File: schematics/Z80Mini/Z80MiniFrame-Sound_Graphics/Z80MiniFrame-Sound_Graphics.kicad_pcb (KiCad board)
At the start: 2 copper layers, 194.3 x 105.4 mm, 48 parts, among them J1 Conn_02x20_Odd_Even, J2 COMP_VIDEOUT, J3 Conn_01x03_Male, J4 IO_PORT, J5 COMP_VIDEOIN, Q1 2N3904, U1 TMS9918A, U12 74LS32, U2 74LS574, U3 74LS574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

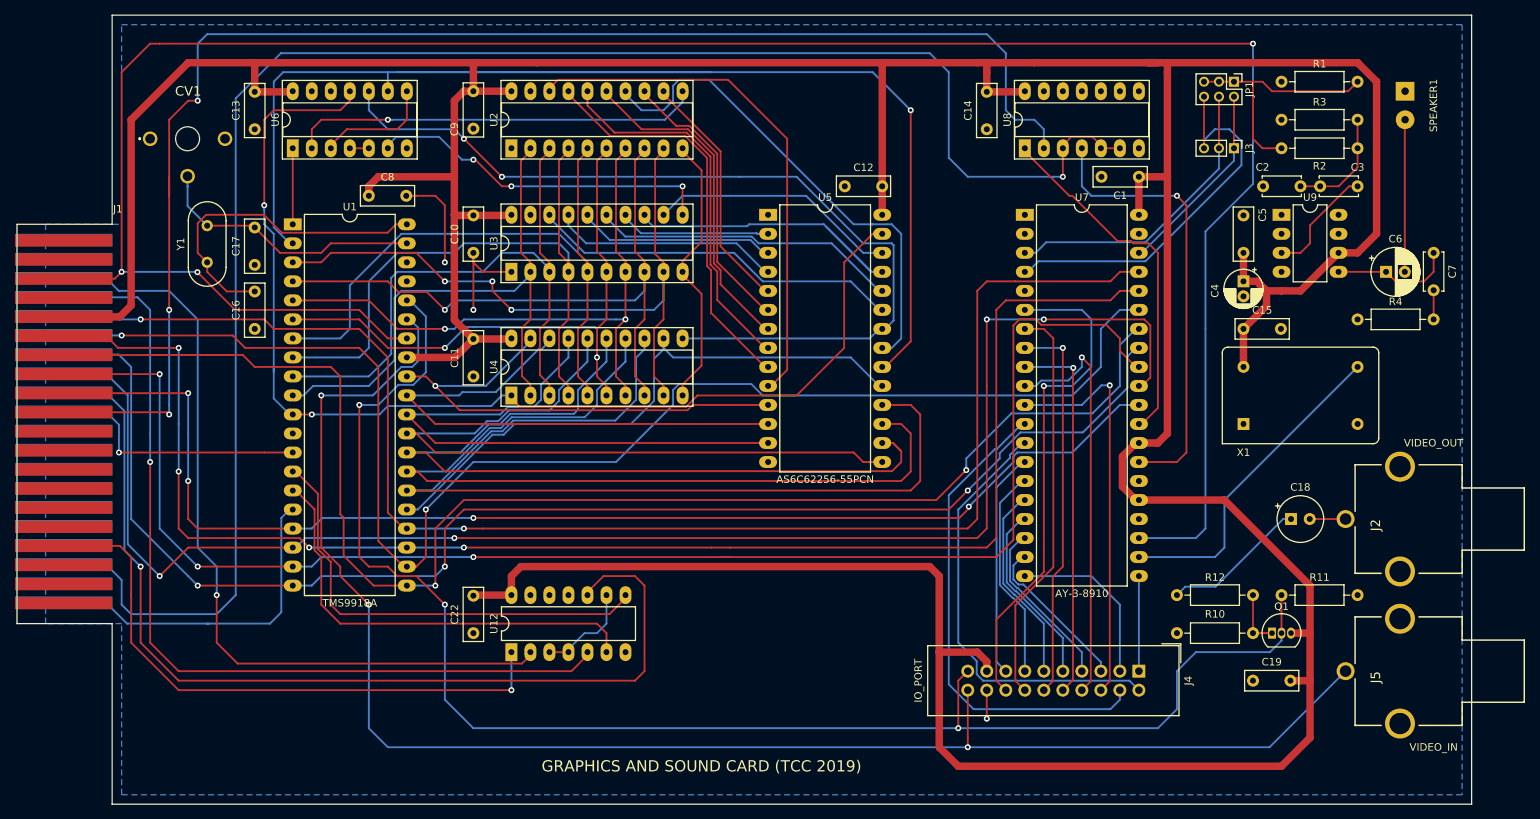
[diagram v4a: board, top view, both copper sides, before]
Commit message: Added new code for core written in C with Z88DK
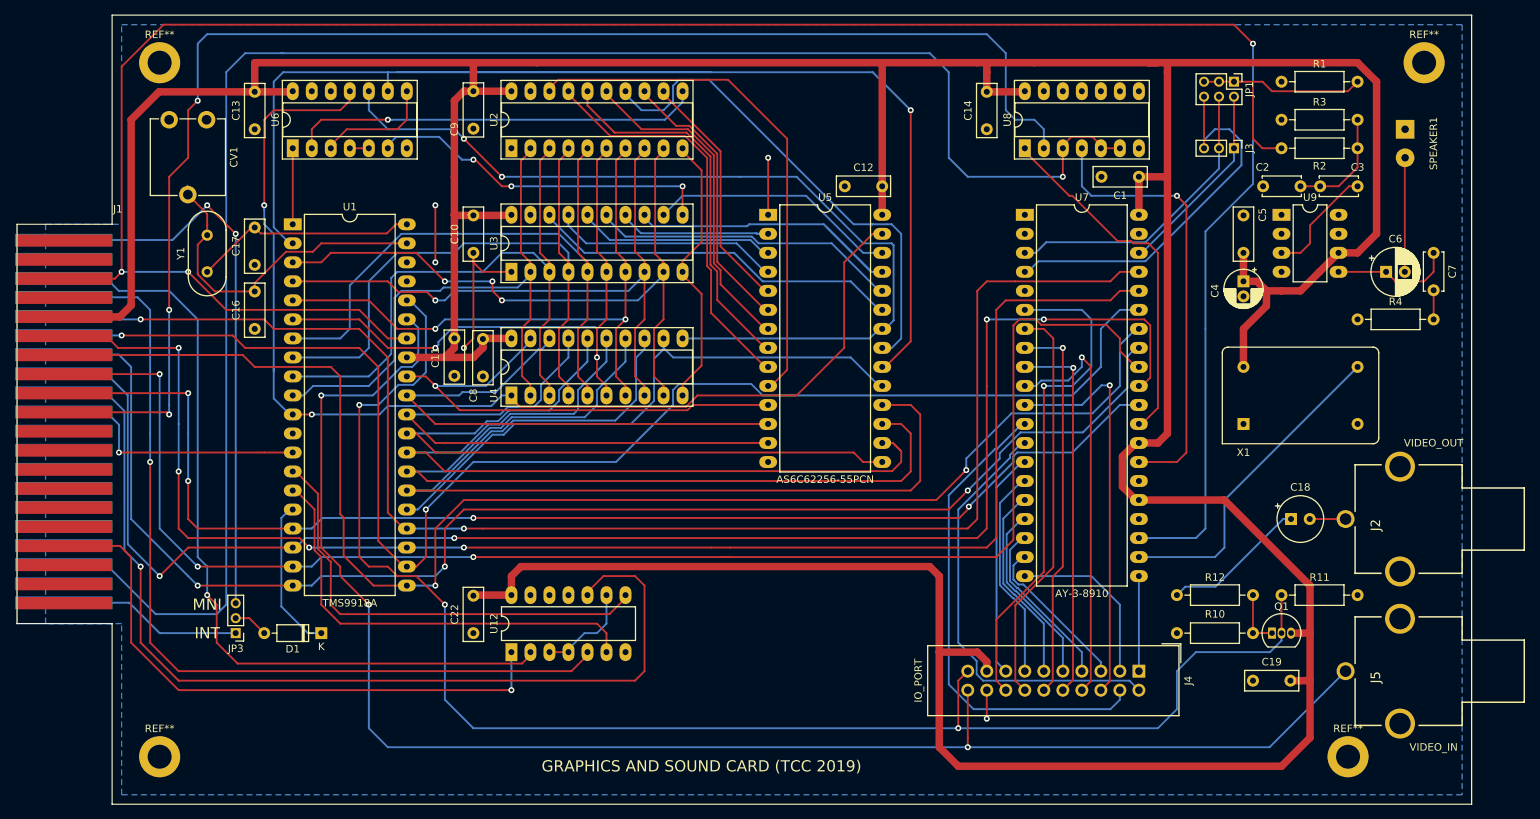
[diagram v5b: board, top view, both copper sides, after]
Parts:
- removed C15: 100nF, Capacitor_THT:C_Disc_D7.0mm_W2.5mm_P5.00mm
- added D1: 1N4148, Diode_THT:D_DO-35_SOD27_P7.62mm_Horizontal, F.Cu at (86.4, 124.5)
- added JP3: Jumper_NC_Dual, Connector_PinHeader_2.00mm:PinHeader_1x03_P2.00mm_Vertical, F.Cu at (74.9, 124.5)
- added REF**: MountingHole_3.2mm_M3_ISO14580_Pad, MountingHole:MountingHole_3.2mm_M3_ISO14580_Pad, F.Cu at (64.8, 48.3)
- added REF**: MountingHole_3.2mm_M3_ISO14580_Pad, MountingHole:MountingHole_3.2mm_M3_ISO14580_Pad, F.Cu at (223.5, 141.0)
- added REF**: MountingHole_3.2mm_M3_ISO14580_Pad, MountingHole:MountingHole_3.2mm_M3_ISO14580_Pad, F.Cu at (233.7, 48.3)
- added REF**: MountingHole_3.2mm_M3_ISO14580_Pad, MountingHole:MountingHole_3.2mm_M3_ISO14580_Pad, F.Cu at (64.8, 141.0)
- CV1: footprint Capacitor_THT:BFC280831659 -> Potentiometer_THT:Potentiometer_ACP_CA9-V10_Vertical
- moved C8 22.2 mm to (104.1, 85.1), turned to 270 degrees
- moved SPEAKER1 5.08 mm to (231.1, 57.1)
- moved CV1 3.59 mm to (66.0, 55.9), turned to 270 degrees
- moved C11 1.27 mm to (108.0, 90.2)
- moved Y1 1.27 mm to (71.1, 76.2)
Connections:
- CV1 pad 2: Net-(C17-Pad2) -> Net-(C16-Pad2)
- CV1 pad 3: GND -> (no net)
- J1 pad 40: /graphicsProcessor/INT -> Net-(J1-Pad40)
- U1 pad 16: /graphicsProcessor/INT -> Net-(D1-Pad1)
- U1 pad 39: Net-(C17-Pad2) -> Net-(C16-Pad2)
- U1 pad 40: Net-(C16-Pad2) -> Net-(C17-Pad2)
- U5 pad 1: Net-(U5-Pad1) -> GND
- Y1 pad 1: Net-(C16-Pad2) -> Net-(C17-Pad2)
- Y1 pad 2: Net-(C17-Pad2) -> Net-(C16-Pad2)
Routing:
- net Net-(J1-Pad2): track 0.00 -> 76.5 mm, vias 0 -> 2
- net /graphicsProcessor/INT: track 51.9 -> 4.64 mm
- net Net-(J1-Pad40): track 0.00 -> 36.6 mm
- net Net-(D1-Pad1): track 0.00 -> 20.6 mm
- net VCC: track 662.2 -> 648.3 mm
- net GND: track 69.6 -> 77.2 mm, vias 3 -> 5
- net Net-(C17-Pad2): track 36.6 -> 30.4 mm
- net Net-(C6-Pad2): track 20.3 -> 15.3 mm
- net /soundGeneration/A0: track 200.1 -> 196.8 mm
- net /graphicsProcessor/AD7: track 93.7 -> 90.6 mm
- net /graphicsProcessor/RESET: track 306.1 -> 308.6 mm
- net /graphicsProcessor/AD6: track 87.3 -> 85.0 mm
- net /soundGeneration/SND_SEL: track 235.1 -> 236.3 mm
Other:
- board text added: "INT"
- board text added: "MNI"

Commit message: Testing C routines for VDP and keyboard. Generated backplane gerber files
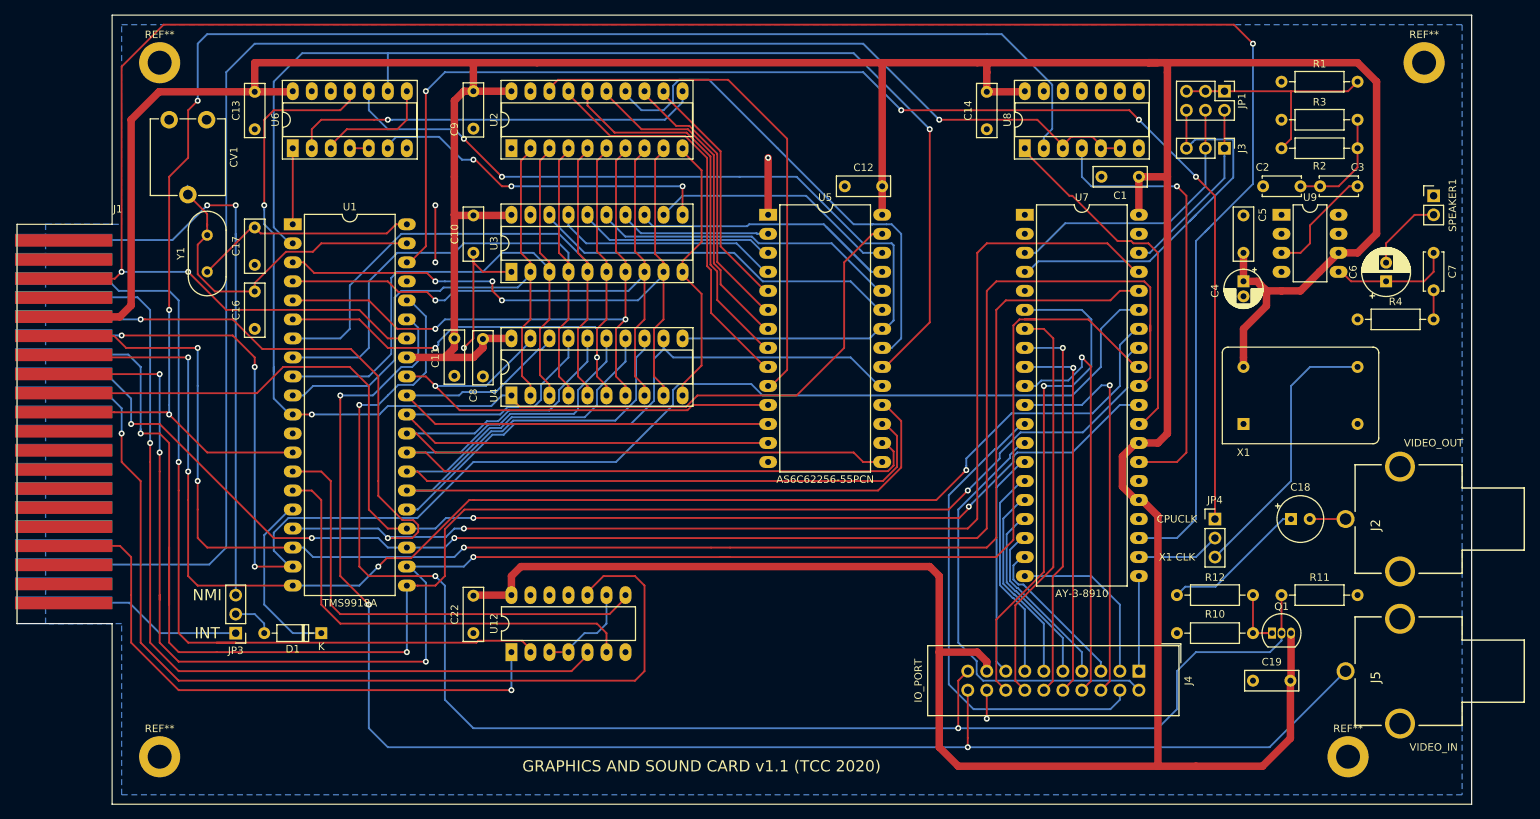
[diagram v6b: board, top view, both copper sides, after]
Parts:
- added ?: , , F.Cu at (207.0, 106.7)
- added JP4: Jumper_NC_Dual, Connector_PinHeader_2.54mm:PinHeader_1x03_P2.54mm_Vertical, F.Cu at (205.7, 109.2)
- J3, JP3: footprint Connector_PinHeader_2.00mm:PinHeader_1x03_P2.00mm_Vertical -> Connector_PinHeader_2.54mm:PinHeader_1x03_P2.54mm_Vertical
- JP1: footprint Connector_PinHeader_2.00mm:PinHeader_2x03_P2.00mm_Vertical -> Connector_PinHeader_2.54mm:PinHeader_2x03_P2.54mm_Vertical
- SPEAKER1: footprint Connector_Wire:SolderWirePad_1x02_P3.81mm_Drill1mm -> Connector_PinHeader_2.54mm:PinHeader_1x02_P2.54mm_Vertical
- moved SPEAKER1 9.67 mm to (234.9, 66.0), turned to 0 degrees
- moved JP1 1.80 mm to (207.0, 52.1)
- moved J3 1.27 mm to (207.0, 59.7)
- moved C6 1.27 mm to (228.6, 77.5), turned to 90 degrees
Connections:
- J1 pad 19: /soundGeneration/A0 -> /graphicsProcessor/A0
- J1 pad 20: /graphicsProcessor/A1 -> Net-(J1-Pad20)
- U1 pad 13: /graphicsProcessor/A1 -> /graphicsProcessor/A0
- U1 pad 17: /D7 -> /D0
- U1 pad 18: /D6 -> /D1
- U1 pad 19: /D5 -> /D2
- U1 pad 20: /D4 -> /D3
- U1 pad 21: /D3 -> /D4
- U1 pad 22: /D2 -> /D5
- U1 pad 23: /D1 -> /D6
- U1 pad 24: /D0 -> /D7
- U1 pad 38: Net-(U1-Pad38) -> /graphicsProcessor/CPUCLK
- U7 pad 22: Net-(U7-Pad22) -> Net-(JP4-Pad2)
- U8 pad 2: /soundGeneration/A0 -> /graphicsProcessor/A0
- X1 pad 8: Net-(U7-Pad22) -> Net-(JP4-Pad3)
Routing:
- net /graphicsProcessor/A0: track 0.00 -> 216.0 mm, vias 0 -> 3
- net /soundGeneration/A0: track 196.8 -> 0.00 mm, vias 3 -> 0
- net /graphicsProcessor/CPUCLK: track 0.00 -> 180.6 mm, vias 0 -> 4
- net Net-(U7-Pad22): track 43.5 -> 0.00 mm
- net Net-(JP4-Pad3): track 0.00 -> 37.0 mm
- net /graphicsProcessor/A1: track 35.5 -> 0.00 mm, vias 1 -> 0
- net Net-(U1-Pad2): track 191.9 -> 156.8 mm
- net /D5: track 202.5 -> 234.4 mm, vias 3 -> 4
- net /D4: track 188.1 -> 217.2 mm
- net /D0: track 199.6 -> 225.8 mm, vias 2 -> 3
- net /soundGeneration/SND_SEL: track 236.3 -> 220.5 mm
- net /D3: track 210.0 -> 197.5 mm, vias 2 -> 4
- net Net-(JP4-Pad2): track 0.00 -> 11.2 mm
- net /D1: track 201.9 -> 209.4 mm, vias 4 -> 3
- net /graphicsProcessor/VD6: track 128.3 -> 121.3 mm
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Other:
- board text added: "CPUCLK"
- board text added: "GRAPHICS AND SOUND CARD v1.1 (TCC 2020)"
- board text added: "NMI"
- board text added: "X1 CLK"
- board text removed: "GRAPHICS AND SOUND CARD (TCC 2019)"
- board text removed: "MNI"
